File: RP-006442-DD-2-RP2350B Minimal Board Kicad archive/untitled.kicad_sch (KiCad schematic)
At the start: 4 parts, among them J1 USB_C_Receptacle_USB2.0_16P, U6 RP2040

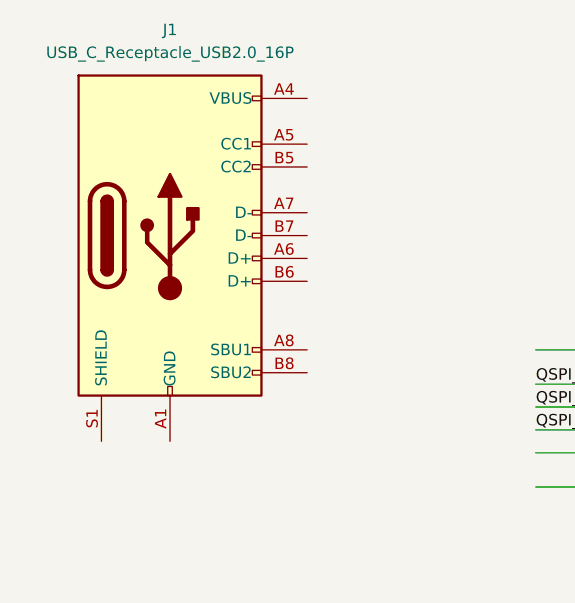
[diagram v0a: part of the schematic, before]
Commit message: added usb-c to pcb editor
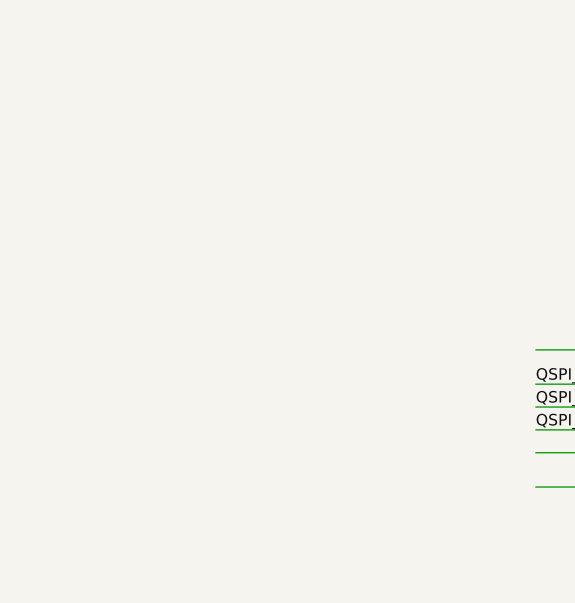
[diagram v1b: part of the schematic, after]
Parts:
- removed J1: USB_C_Receptacle_USB2.0_16P, Connector_USB:USB_C_Receptacle_HRO_TYPE-C-31-M-12, symbol Connector:USB_C_Receptacle_USB2.0_16P
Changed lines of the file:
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@@
-		)
-	)
-	(symbol
-		(lib_id "Connector:USB_C_Receptacle_USB2.0_16P")
-		(at 40.64 58.42 0)
-		(unit 1)
-		(exclude_from_sim no)
-		(in_bom yes)
-		(on_board yes)
-		(dnp no)
-		(fields_autoplaced yes)
-		(property "Reference" "J1"
-			(at 40.64 35.56 0)
-			(effects
-				(font
-					(size 1.27 1.27)
-				)
-			)
-		)
-		(property "Value" "USB_C_Receptacle_USB2.0_16P"
-			(at 40.64 38.1 0)
-			(effects
-				(font
-					(size 1.27 1.27)
-				)
-			)
-		)
-		(property "Footprint" "Connector_USB:USB_C_Receptacle_HRO_TYPE-C-31-M-12"
-			(at 44.45 58.42 0)
-			(effects
-				(font
-					(size 1.27 1.27)
-				)
-				(hide yes)
-			)
-		)
-		(property "Datasheet" "https://www.usb.org/sites/default/files/documents/usb_type-c.zip"
-			(at 44.45 58.42 0)
-			(effects
-				(font
-					(size 1.27 1.27)
-				)
-				(hide yes)
-			)
-		)
-		(property "Description" "USB 2.0-only 16P Type-C Receptacle connector"
-			(at 40.64 58.42 0)
-			(effects
-				(font
-					(size 1.27 1.27)
-				)
-				(hide yes)
-			)
-		)
-		(pin "B7"
-		)
-		(pin "B8"
-		)
-		(pin "A12"
-		)
-		(pin "B4"
-		)
-		(pin "A8"
-		)
-		(pin "A5"
-		)
-		(pin "A9"
-		)
-		(pin "S1"
-		)
-		(pin "B6"
-		)
-		(pin "B12"
-		)
-		(pin "A1"
-		)
-		(pin "B1"
-		)
-		(pin "A4"
-		)
-		(pin "A6"
-		)
-		(pin "B9"
-		)
-		(pin "B5"
-		)
-		(pin "A7"
-		)
-		(instances
-			(project "RP2350_80QFN_minimal"
-				(path "/94683f5c-9cd9-448e-be96-9792537b5cb8/d9764033-4a4d-4e32-b4ec-d607be2f0d91"
-					(reference "J1")
-					(unit 1)
-				)
-			)
 		)
 	)
